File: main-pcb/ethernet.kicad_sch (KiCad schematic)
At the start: 79 parts, among them J6 0826-1G1T-23-F, Q1 SSM6N58NU, U1 XC7S100-1FGGA484C, U17 S27KS0642GABHI030, U18 ECS-1612MV-250-CN, U20 KSZ9031RN, U21 RCLAMP0514M, U22 RCLAMP0514M, U24 IS25WP256D-JLLE

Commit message: Initial design mostly done aside from USB connector, review, test points
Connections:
- net A3V3 is gone; now on net A2V5: U21.3 (Vcc), U22.3 (Vcc)
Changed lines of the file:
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@@
 	(title_block
 		(title "DUMPTRUCK flash dumper")
-		(date "2024-10-14")
+		(date "2024-10-16")
 		(rev "0.1")
 		(company "Antikernel Labs")
@@
 		)
 	)
-	(label "A3V3"
+	(label "A2V5"
 		(at 203.2 166.37 180)
 		(fields_autoplaced yes)
@@
 		)
 	)
-	(label "A3V3"
+	(label "A2V5"
 		(at 203.2 130.81 180)
 		(fields_autoplaced yes)
@@
 		(pin "P9"
 		)
-		(pin ""
-		)
 		(pin "V12"

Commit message: Finished initial schematic pass, ready for review
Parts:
- added R105, R106: 10K, azonenberg_pcb:EIA_0402_RES_NOSILK, symbol device:R
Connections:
- net 1V8: now also U1.M19 (IO_L3P_T0_DQS_PUDC_B_14), R105.1, R106.1
- net FPGA_RAM_CS_N: now also R105.2
- net FPGA_RAM_RST_N: now also R106.2
- no-connect marks 14 -> 13
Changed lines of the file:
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@@
 	)
 	(no_connect
-		(at 340.36 35.56)
-	)
-	(no_connect
 		(at 340.36 147.32)
 	)
@@
 	(wire
 		(pts
+			(xy 351.79 212.09) (xy 355.6 212.09)
+		)
+		(stroke
+			(width 0)
+			(type default)
+		)
+	)
+	(wire
+		(pts
 			(xy 110.49 34.29) (xy 110.49 36.83)
 		)
@@
 	(wire
 		(pts
+			(xy 351.79 205.74) (xy 355.6 205.74)
+		)
+		(stroke
+			(width 0)
+			(type default)
+		)
+	)
+	(wire
+		(pts
 			(xy 214.63 208.28) (xy 234.95 208.28)
 		)
@@
 		)
 	)
+	(label "FPGA_RAM_RST_N"
+		(at 355.6 212.09 0)
+		(fields_autoplaced yes)
+		(effects
+			(font
+				(size 1.27 1.27)
+			)
+			(justify left bottom)
+		)
+	)
 	(label "ETH_LED1_N_1V8"
 		(at 340.36 124.46 180)
@@
 		)
 	)
+	(label "FPGA_RAM_CS_N"
+		(at 355.6 205.74 0)
+		(fields_autoplaced yes)
+		(effects
+			(font
+				(size 1.27 1.27)
+			)
+			(justify left bottom)
+		)
+	)
 	(label "1V8"
 		(at 189.23 86.36 0)
@@
 		)
 	)
+	(label "1V8"
+		(at 340.36 35.56 180)
+		(fields_autoplaced yes)
+		(effects
+			(font
+				(size 1.27 1.27)
+			)
+			(justify right bottom)
+		)
+	)
 	(label "RGMII_TXD1"
 		(at 167.64 49.53 0)
@@
 		)
 	)
+	(label "1V8"
+		(at 344.17 205.74 180)
+		(fields_autoplaced yes)
+		(effects
+			(font
+				(size 1.27 1.27)
+			)
+			(justify right bottom)
+		)
+	)
 	(label "FPGA_RAM_DQ4"
 		(at 375.92 173.99 0)
@@
 		)
 	)
+	(label "1V8"
+		(at 344.17 212.09 180)
+		(fields_autoplaced yes)
+		(effects
+			(font
+				(size 1.27 1.27)
+			)
+			(justify right bottom)
+		)
+	)
 	(label "ETH_RX_DV"
 		(at 185.42 73.66 0)
@@
 	)
 	(symbol
+		(lib_id "device:R")
+		(at 347.98 212.09 90)
+		(unit 1)
+		(exclude_from_sim no)
+		(in_bom yes)
+		(on_board yes)
+		(dnp no)
+		(property "Reference" "R106"
+			(at 347.98 209.55 90)
+			(effects
+				(font
+					(size 1.27 1.27)
+				)
+			)
+		)
+		(property "Value" "10K"
+			(at 347.98 212.09 90)
+			(effects
+				(font
+					(size 1.27 1.27)
+				)
+			)
+		)
+		(property "Footprint" "azonenberg_pcb:EIA_0402_RES_NOSILK"
+			(at 347.98 213.868 90)
+			(effects
+				(font
+					(size 1.27 1.27)
+				)
+				(hide yes)
+			)
+		)
+		(property "Datasheet" ""
+			(at 347.98 212.09 0)
+			(effects
+				(font
+					(size 1.27 1.27)
+				)
+				(hide yes)
+			)
+		)
+		(property "Description" ""
+			(at 347.98 212.09 0)
+			(effects
+				(font
+					(size 1.27 1.27)
+				)
+				(hide yes)
+			)
+		)
+		(pin "1"
+		)
+		(pin "2"
+		)
+		(instances
+			(project "main-pcb"
+				(path "/e33e9f2b-a48c-455d-96ec-c7304b1720d3/0a1e5a7c-b848-45cd-a3bc-e7f3bda10553"
+					(reference "R106")
+					(unit 1)
+				)
+			)
+		)
+	)
+	(symbol
 		(lib_id "passive-azonenberg:FERRITE_SMALL2")
 		(at 74.93 190.5 0)
@@
 					(unit 1)
 				)
+			)
+		)
+	)
+	(symbol
+		(lib_id "device:R")
+		(at 347.98 205.74 90)
+		(unit 1)
+		(exclude_from_sim no)
+		(in_bom yes)
+		(on_board yes)
+		(dnp no)
+		(property "Reference" "R105"
+			(at 347.98 203.2 90)
+			(effects
+				(font
+					(size 1.27 1.27)
+				)
+			)
+		)
+		(property "Value" "10K"
+			(at 347.98 205.74 90)
+			(effects
+				(font
+					(size 1.27 1.27)
+				)
+			)
+		)
+		(property "Footprint" "azonenberg_pcb:EIA_0402_RES_NOSILK"
+			(at 347.98 207.518 90)
+			(effects
+				(font
+					(size 1.27 1.27)
+				)
+				(hide yes)
+			)
+		)
+		(property "Datasheet" ""
+			(at 347.98 205.74 0)
+			(effects
+				(font
+					(size 1.27 1.27)
+				)
+				(hide yes)
+			)
+		)
+		(property "Description" ""
+			(at 347.98 205.74 0)
+			(effects
+				(font
+					(size 1.27 1.27)
+				)
+				(hide yes)
+			)
+		)
+		(pin "1"
+		)
+		(pin "2"
+		)
+		(instances
+			(project "main-pcb"
+				(path "/e33e9f2b-a48c-455d-96ec-c7304b1720d3/0a1e5a7c-b848-45cd-a3bc-e7f3bda10553"
+					(reference "R105")
+					(unit 1)
+				)

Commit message: More schematic tweaks and test points
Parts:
- Q1: footprint (none) -> azonenberg_pcb:DFN_6_0.65MM_2x2MM_GDS
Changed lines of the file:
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@@
 			)
 		)
-		(property "Footprint" ""
+		(property "Footprint" "azonenberg_pcb:DFN_6_0.65MM_2x2MM_GDS"
 			(at 274.32 176.53 0)
 			(effects
@@
 			)
 		)
-		(property "Footprint" ""
+		(property "Footprint" "azonenberg_pcb:DFN_6_0.65MM_2x2MM_GDS"
 			(at 274.32 157.48 0)
 			(effects

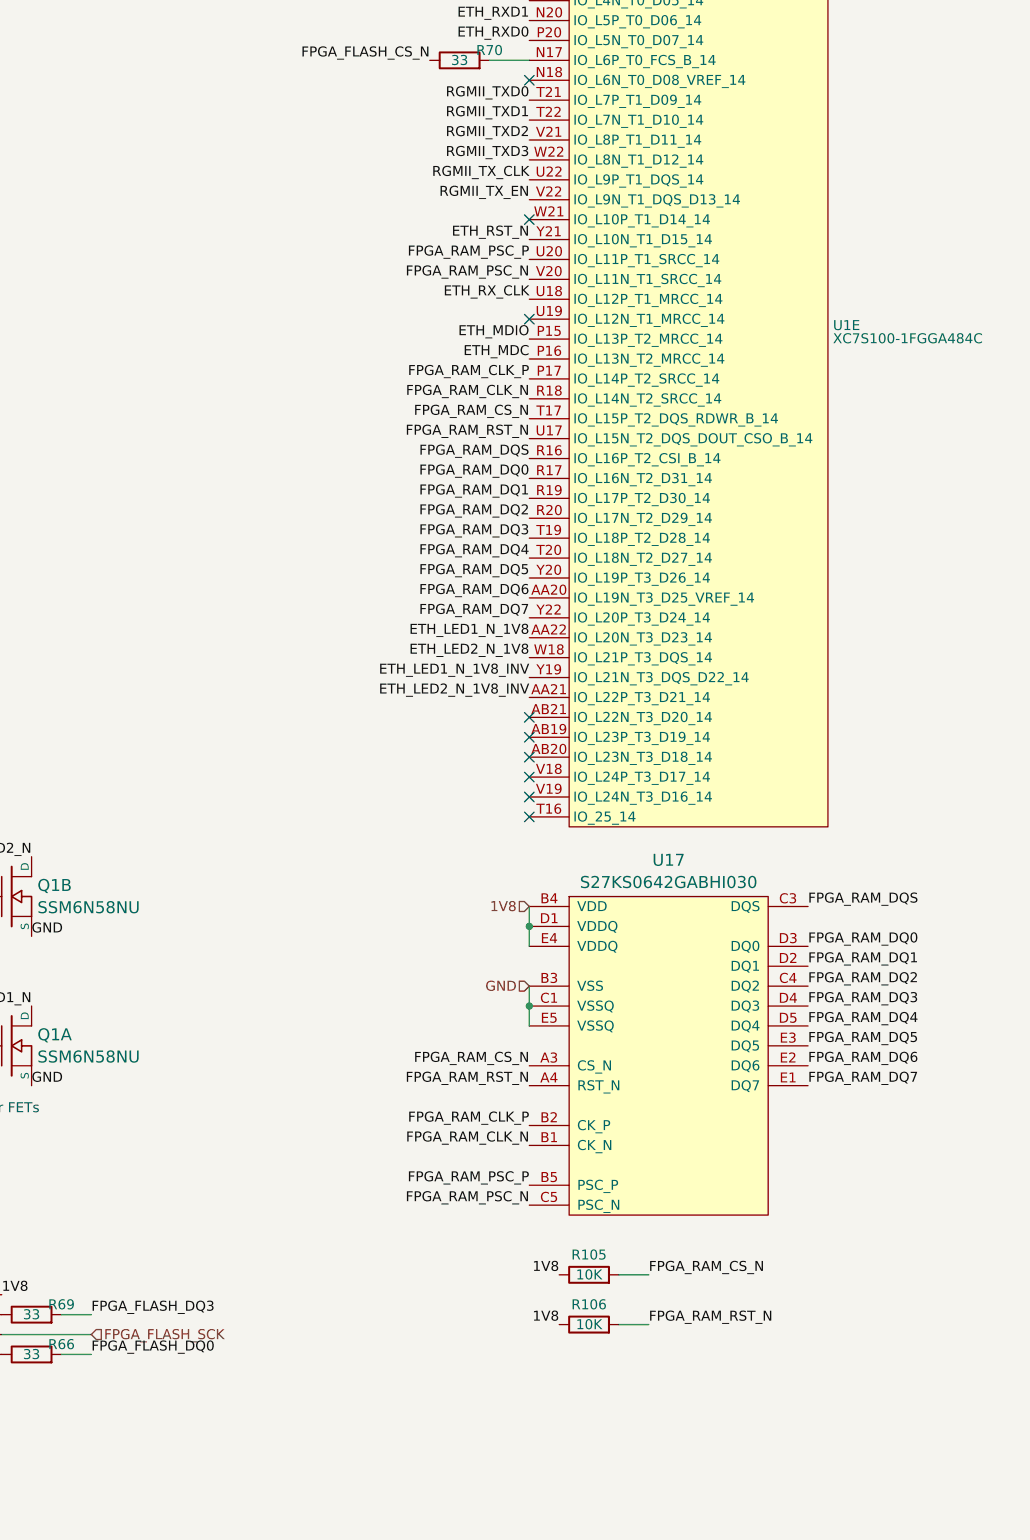
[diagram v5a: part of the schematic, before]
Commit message: Continued layout mostly of DUT connectors
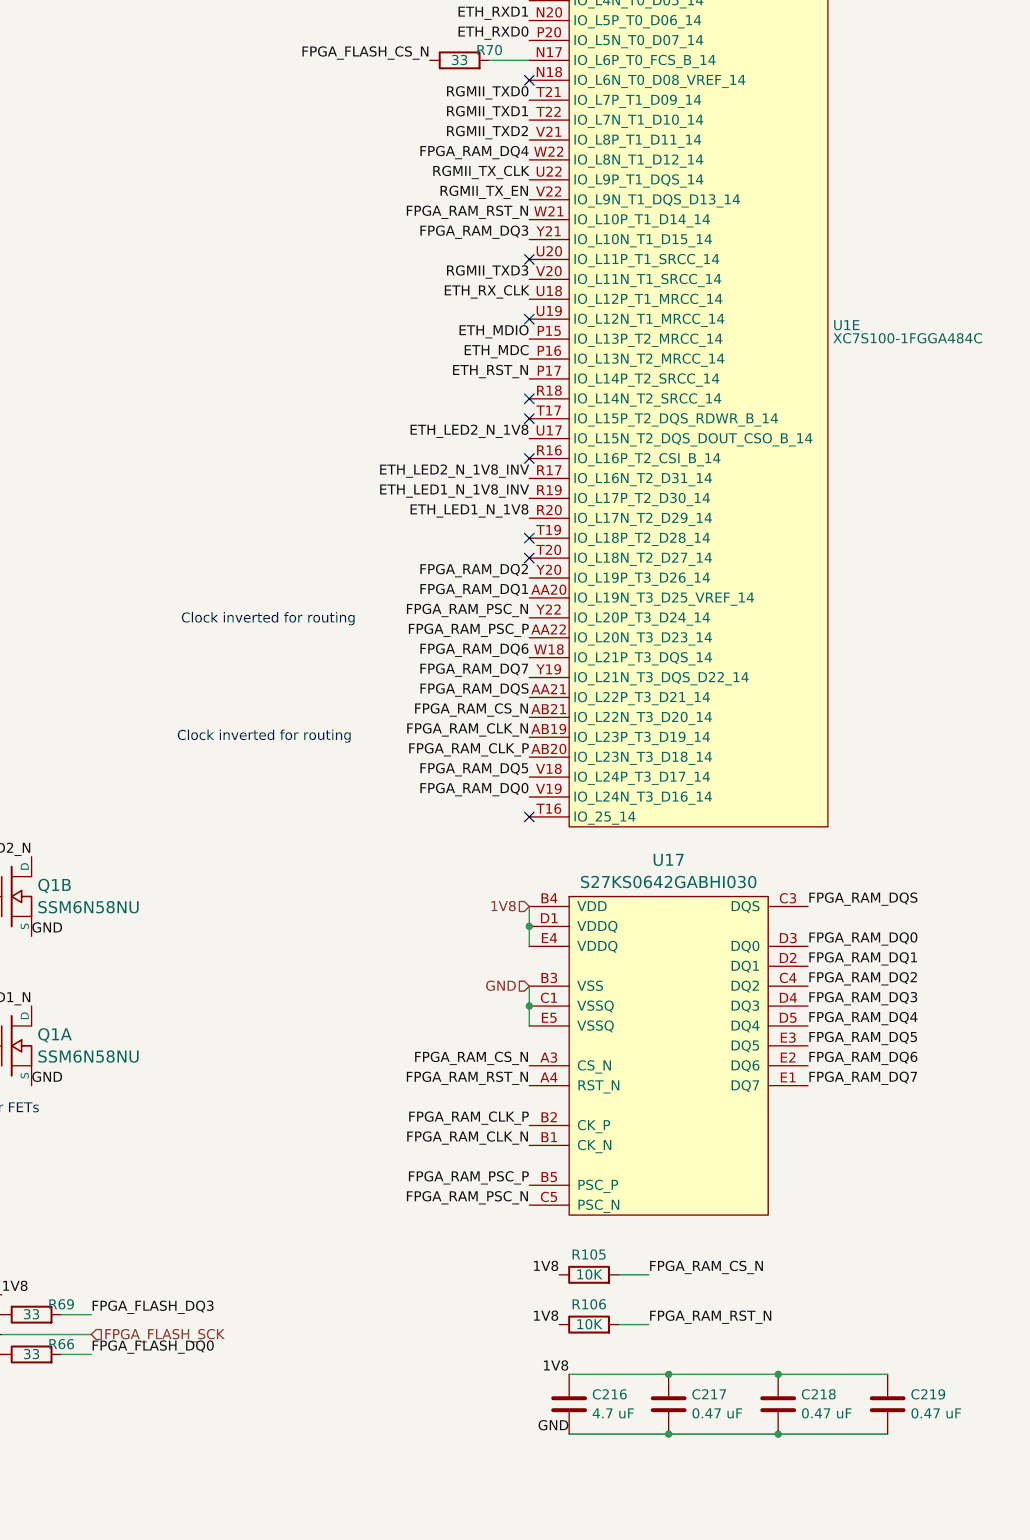
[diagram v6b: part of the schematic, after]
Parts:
- added C216: 4.7 uF, azonenberg_pcb:EIA_0603_CAP_NOSILK, symbol device:C
- added C217, C218, C219: 0.47 uF, azonenberg_pcb:EIA_0402_CAP_NOSILK, symbol device:C
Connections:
- net 1V8: now also C216.1, C217.1, C218.1, C219.1
- net ETH_LED1_N_1V8: now also U1.R20 (IO_L17N_T2_D29_14); no longer U1.AA22 (IO_L20N_T3_D23_14)
- net ETH_LED1_N_1V8_INV: now also U1.R19 (IO_L17P_T2_D30_14); no longer U1.Y19 (IO_L21N_T3_DQS_D22_14)
- net ETH_LED2_N_1V8: now also U1.U17 (IO_L15N_T2_DQS_DOUT_CSO_B_14); no longer U1.W18 (IO_L21P_T3_DQS_14)
- net ETH_LED2_N_1V8_INV: now also U1.R17 (IO_L16N_T2_D31_14); no longer U1.AA21 (IO_L22P_T3_D21_14)
- net ETH_RST_N: now also U1.P17 (IO_L14P_T2_SRCC_14); no longer U1.Y21 (IO_L10N_T1_D15_14)
- net FPGA_RAM_CLK_N: now also U1.AB19 (IO_L23P_T3_D19_14); no longer U1.R18 (IO_L14N_T2_SRCC_14)
- net FPGA_RAM_CLK_P: now also U1.AB20 (IO_L23N_T3_D18_14); no longer U1.P17 (IO_L14P_T2_SRCC_14)
- net FPGA_RAM_CS_N: now also U1.AB21 (IO_L22N_T3_D20_14); no longer U1.T17 (IO_L15P_T2_DQS_RDWR_B_14)
- net FPGA_RAM_DQ0: now also U1.V19 (IO_L24N_T3_D16_14); no longer U1.R17 (IO_L16N_T2_D31_14)
- net FPGA_RAM_DQ1: now also U1.AA20 (IO_L19N_T3_D25_VREF_14); no longer U1.R19 (IO_L17P_T2_D30_14)
- net FPGA_RAM_DQ2: now also U1.Y20 (IO_L19P_T3_D26_14); no longer U1.R20 (IO_L17N_T2_D29_14)
- net FPGA_RAM_DQ3: now also U1.Y21 (IO_L10N_T1_D15_14); no longer U1.T19 (IO_L18P_T2_D28_14)
- net FPGA_RAM_DQ4: now also U1.W22 (IO_L8N_T1_D12_14); no longer U1.T20 (IO_L18N_T2_D27_14)
- net FPGA_RAM_DQ5: now also U1.V18 (IO_L24P_T3_D17_14); no longer U1.Y20 (IO_L19P_T3_D26_14)
- net FPGA_RAM_DQ6: now also U1.W18 (IO_L21P_T3_DQS_14); no longer U1.AA20 (IO_L19N_T3_D25_VREF_14)
- net FPGA_RAM_DQ7: now also U1.Y19 (IO_L21N_T3_DQS_D22_14); no longer U1.Y22 (IO_L20P_T3_D24_14)
- net FPGA_RAM_DQS: now also U1.AA21 (IO_L22P_T3_D21_14); no longer U1.R16 (IO_L16P_T2_CSI_B_14)
- net FPGA_RAM_PSC_N: now also U1.Y22 (IO_L20P_T3_D24_14); no longer U1.V20 (IO_L11N_T1_SRCC_14)
- net FPGA_RAM_PSC_P: now also U1.AA22 (IO_L20N_T3_D23_14); no longer U1.U20 (IO_L11P_T1_SRCC_14)
- net FPGA_RAM_RST_N: now also U1.W21 (IO_L10P_T1_D14_14); no longer U1.U17 (IO_L15N_T2_DQS_DOUT_CSO_B_14)
- net GND: now also C216.2, C217.2, C218.2, C219.2
- net RGMII_TXD3: now also U1.V20 (IO_L11N_T1_SRCC_14); no longer U1.W22 (IO_L8N_T1_D12_14)
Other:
- note added: "Clock inverted for routing"

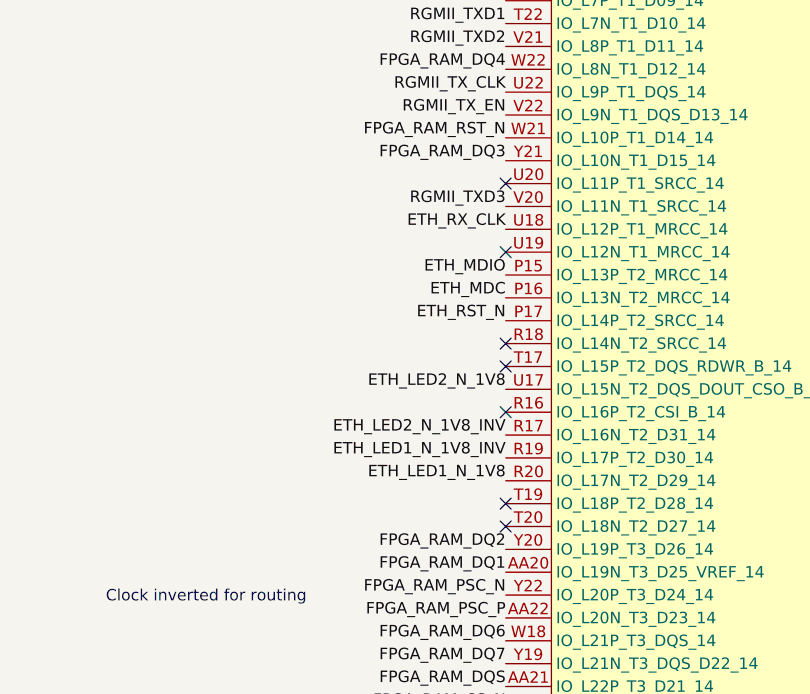
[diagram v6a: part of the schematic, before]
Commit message: Continued routing MCU, started work on PHY
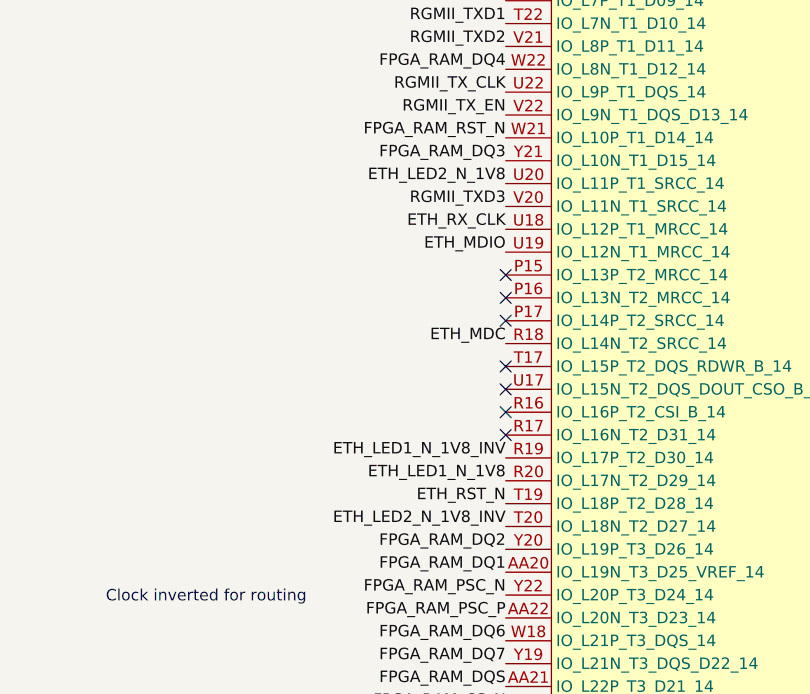
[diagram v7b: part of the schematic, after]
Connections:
- net ETH_LED2_N_1V8: now also U1.U20 (IO_L11P_T1_SRCC_14); no longer U1.U17 (IO_L15N_T2_DQS_DOUT_CSO_B_14)
- net ETH_LED2_N_1V8_INV: now also U1.T20 (IO_L18N_T2_D27_14); no longer U1.R17 (IO_L16N_T2_D31_14)
- net ETH_MDC: now also U1.R18 (IO_L14N_T2_SRCC_14); no longer U1.P16 (IO_L13N_T2_MRCC_14)
- net ETH_MDIO: now also U1.U19 (IO_L12N_T1_MRCC_14); no longer U1.P15 (IO_L13P_T2_MRCC_14)
- net ETH_RST_N: now also U1.T19 (IO_L18P_T2_D28_14); no longer U1.P17 (IO_L14P_T2_SRCC_14)
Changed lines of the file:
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@@
 	(title_block
 		(title "DUMPTRUCK flash dumper")
-		(date "2024-10-19")
+		(date "2024-10-20")
 		(rev "0.1")
 		(company "Antikernel Labs")
@@
 	)
 	(no_connect
-		(at 340.36 111.76)
+		(at 340.36 88.9)
 	)
 	(no_connect
@@
 	)
 	(no_connect
-		(at 340.36 83.82)
-	)
-	(no_connect
 		(at 167.64 95.25)
-	)
-	(no_connect
-		(at 340.36 114.3)
 	)
 	(no_connect
@@
 	)
 	(no_connect
-		(at 340.36 93.98)
+		(at 340.36 104.14)
 	)
 	(no_connect
-		(at 340.36 76.2)
+		(at 340.36 91.44)
+	)
+	(no_connect
+		(at 340.36 99.06)
 	)
 	(no_connect
@@
 	(no_connect
 		(at 340.36 96.52)
+	)
+	(no_connect
+		(at 340.36 86.36)
 	)
 	(no_connect
@@
 	)
 	(label "ETH_RST_N"
-		(at 340.36 91.44 180)
+		(at 340.36 111.76 180)
 		(fields_autoplaced yes)
 		(effects
@@
 	)
 	(label "ETH_LED2_N_1V8_INV"
-		(at 340.36 104.14 180)
+		(at 340.36 114.3 180)
 		(fields_autoplaced yes)
 		(effects
@@
 	)
 	(label "ETH_LED2_N_1V8"
-		(at 340.36 99.06 180)
+		(at 340.36 76.2 180)
 		(fields_autoplaced yes)
 		(effects
@@
 	)
 	(label "ETH_MDC"
-		(at 340.36 88.9 180)
+		(at 340.36 93.98 180)
 		(fields_autoplaced yes)
 		(effects
@@
 	)
 	(label "ETH_MDIO"
-		(at 340.36 86.36 180)
-		(fields_autoplaced yes)
-		(effects
+		(at 340.36 83.82 180)
+		(fields_autoplaced yes)
+		(effects

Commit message: 500 unrouted, still lots more to go
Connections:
- net 1V8: now also R65.1
- net 3V3: no longer R65.1
- net ETH_LED1_N_1V8: now also U1.T22 (IO_L7N_T1_D10_14); no longer U1.R20 (IO_L17N_T2_D29_14)
- net ETH_LED2_N_1V8: now also U1.R20 (IO_L17N_T2_D29_14); no longer U1.U20 (IO_L11P_T1_SRCC_14)
- net RGMII_TXD1: now also U1.U22 (IO_L9P_T1_DQS_14); no longer U1.T22 (IO_L7N_T1_D10_14)
- net RGMII_TXD2: now also U1.V20 (IO_L11N_T1_SRCC_14); no longer U1.V21 (IO_L8P_T1_D11_14)
- net RGMII_TXD3: now also U1.V22 (IO_L9N_T1_DQS_D13_14); no longer U1.V20 (IO_L11N_T1_SRCC_14)
- net RGMII_TX_CLK: now also U1.V21 (IO_L8P_T1_D11_14); no longer U1.U22 (IO_L9P_T1_DQS_14)
- net RGMII_TX_EN: now also U1.U20 (IO_L11P_T1_SRCC_14); no longer U1.V22 (IO_L9N_T1_DQS_D13_14)
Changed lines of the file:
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@@
 	)
 	(label "RGMII_TXD1"
-		(at 340.36 58.42 180)
+		(at 340.36 66.04 180)
 		(fields_autoplaced yes)
 		(effects
@@
 	)
 	(label "ETH_LED1_N_1V8"
-		(at 340.36 109.22 180)
+		(at 340.36 58.42 180)
 		(fields_autoplaced yes)
 		(effects
@@
 		)
 	)
-	(label "3V3"
+	(label "1V8"
 		(at 233.68 88.9 0)
 		(fields_autoplaced yes)
@@
 	)
 	(label "ETH_LED2_N_1V8"
-		(at 340.36 76.2 180)
+		(at 340.36 109.22 180)
 		(fields_autoplaced yes)
 		(effects
@@
 	)
 	(label "RGMII_TX_EN"
-		(at 340.36 68.58 180)
+		(at 340.36 76.2 180)
 		(fields_autoplaced yes)
 		(effects
@@
 	)
 	(label "RGMII_TX_CLK"
-		(at 340.36 66.04 180)
+		(at 340.36 60.96 180)
 		(fields_autoplaced yes)
 		(effects
@@
 	)
 	(label "RGMII_TXD3"
-		(at 340.36 78.74 180)
+		(at 340.36 68.58 180)
 		(fields_autoplaced yes)
 		(effects
@@
 	)
 	(label "RGMII_TXD2"
-		(at 340.36 60.96 180)
-		(fields_autoplaced yes)
-		(effects
+		(at 340.36 78.74 180)
+		(fields_autoplaced yes)
+		(effects
